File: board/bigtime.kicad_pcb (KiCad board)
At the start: 2 copper layers, 100 x 100 mm, 10 parts, among them IC1 NPIC6C596A, IC2 TPS62152, P1 CONN_IN, P2 CONN_OUT, U1 SA40-19

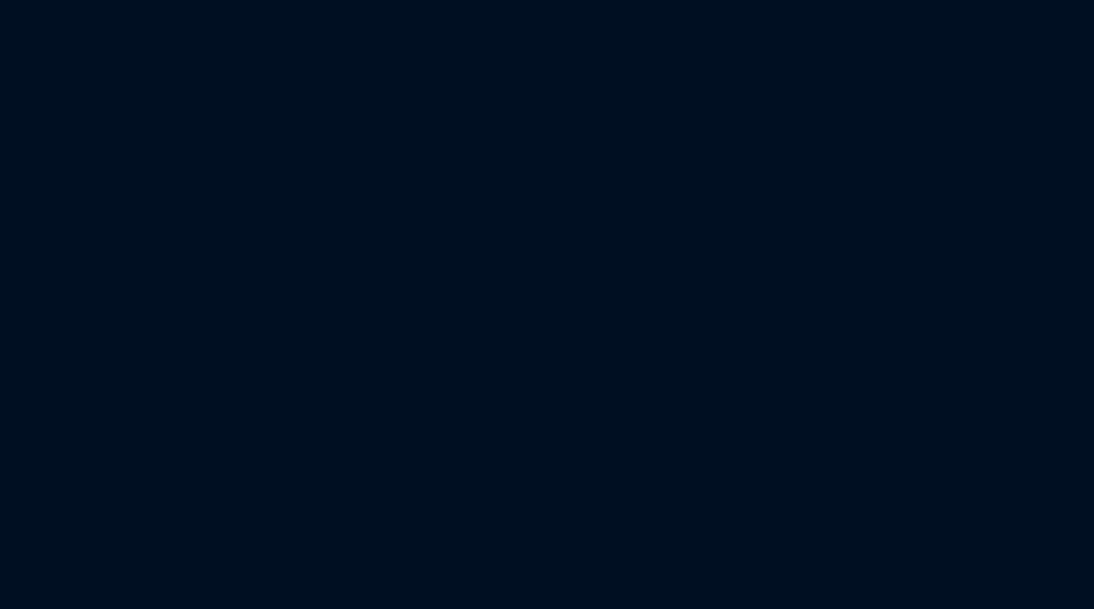
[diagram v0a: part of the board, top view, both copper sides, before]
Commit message: Added limit resistors
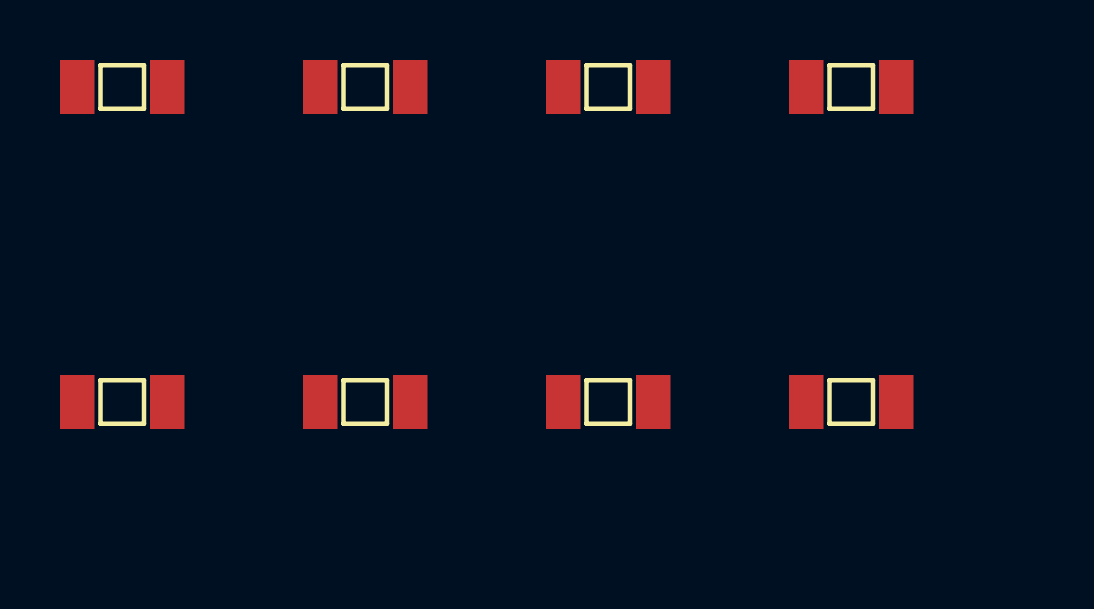
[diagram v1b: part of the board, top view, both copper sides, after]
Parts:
- added R1: 220R 500mW, agg:1206, F.Cu at (109.8, 43.9)
- added R2: 220R 500mW, agg:1206, F.Cu at (85.5, 43.9)
- added R3: 220R 500mW, agg:1206, F.Cu at (93.6, 33.4)
- added R4: 220R 500mW, agg:1206, F.Cu at (101.7, 33.4)
- added R5: 220R 500mW, agg:1206, F.Cu at (93.6, 43.9)
- added R6: 220R 500mW, agg:1206, F.Cu at (85.5, 33.4)
- added R7: 220R 500mW, agg:1206, F.Cu at (101.7, 43.9)
- added R8: 400R 500mW, agg:1206, F.Cu at (109.8, 33.4)
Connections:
- U1 pad 1: Net-(IC1-Pad11) -> Net-(R5-Pad1)
- U1 pad 10: Net-(IC1-Pad13) -> Net-(R7-Pad1)
- U1 pad 2: Net-(IC1-Pad6) -> Net-(R4-Pad1)
- U1 pad 4: Net-(IC1-Pad5) -> Net-(R3-Pad1)
- U1 pad 5: Net-(IC1-Pad14) -> Net-(R8-Pad2)
- U1 pad 6: Net-(IC1-Pad4) -> Net-(R2-Pad1)
- U1 pad 7: Net-(IC1-Pad3) -> Net-(R1-Pad1)
- U1 pad 9: Net-(IC1-Pad12) -> Net-(R6-Pad1)

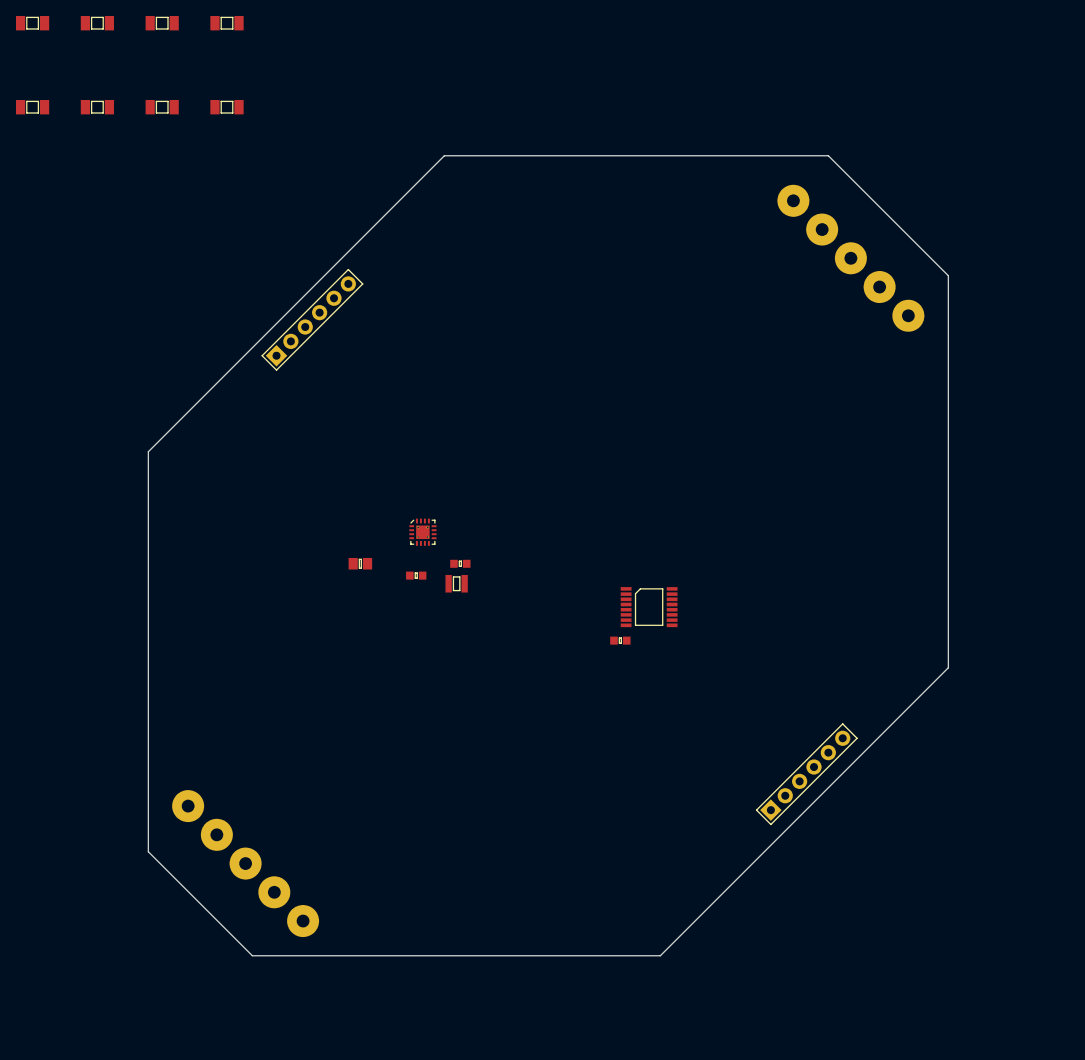
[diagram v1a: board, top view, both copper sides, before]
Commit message: Rectangular board because life's too short
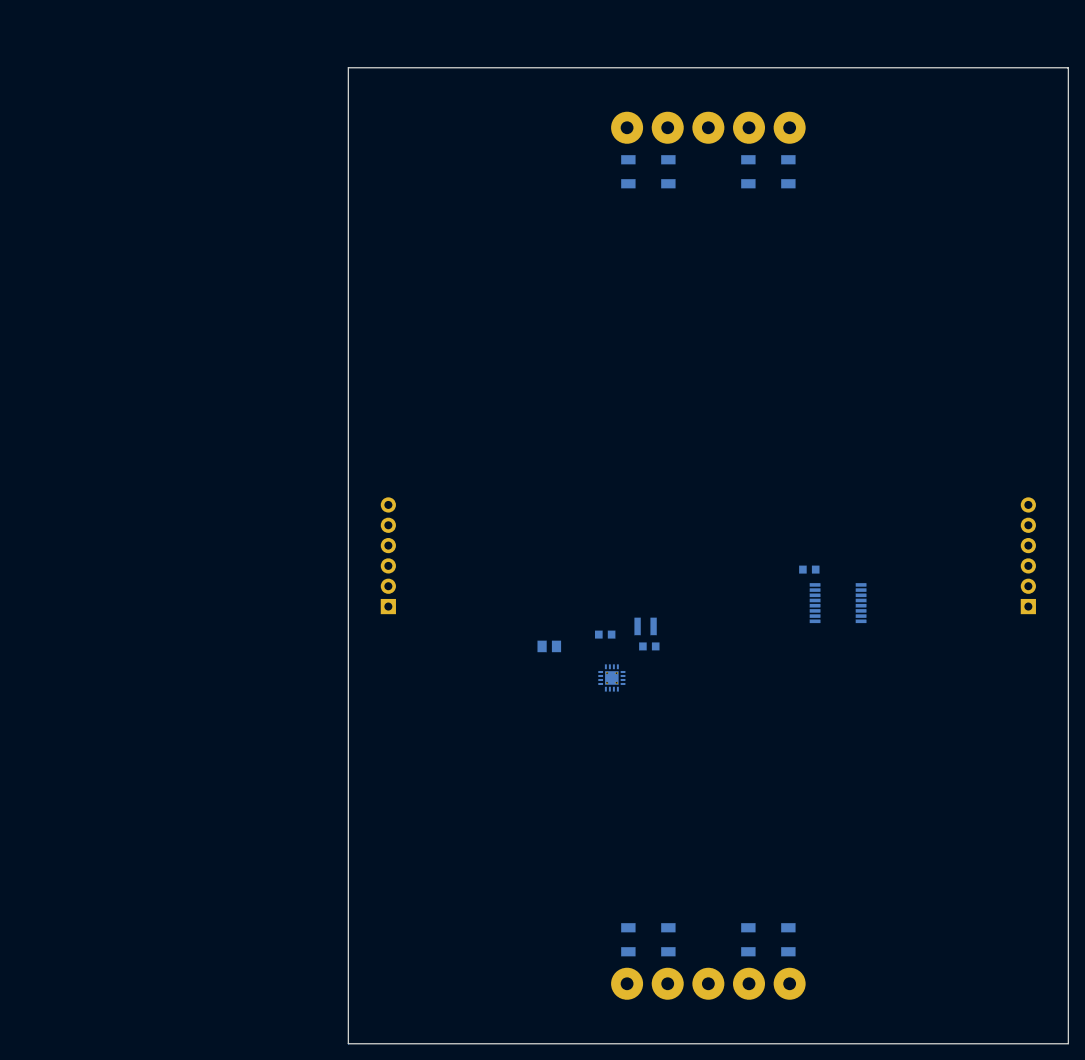
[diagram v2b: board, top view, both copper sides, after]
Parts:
- C1, C2, C3, C4, IC1, IC2, L1, P1, P2, R1, R2, R3, R4, R5, R6, R7, R8: moved to B.Cu
- moved R3 140.5 mm to (175.0, 148.0), turned to 90 degrees
- moved R8 134.4 mm to (180.0, 148.0), turned to 270 degrees
- moved R4 130.9 mm to (165.0, 148.0), turned to 90 degrees
- moved R5 123.4 mm to (160.0, 148.0), turned to 90 degrees
- moved R2 94.8 mm to (180.0, 52.0), turned to 270 degrees
- moved R6 81.6 mm to (165.0, 52.0), turned to 270 degrees
- moved R1 65.7 mm to (175.0, 52.0), turned to 270 degrees
- moved R7 58.8 mm to (160.0, 52.0), turned to 270 degrees
- moved P2 38.9 mm to (210.0, 100.0), turned to 90 degrees
- moved P1 31.0 mm to (130.0, 100.0), turned to 90 degrees
- moved IC2 29.8 mm to (157.9, 115.3)
- moved C3 25.8 mm to (162.6, 111.3)
- moved C4 25.8 mm to (150.1, 111.3)
- moved C1 25.2 mm to (182.6, 101.7)
- moved C2 24.7 mm to (157.1, 109.9)
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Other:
- board size 100 x 100 mm -> 90 x 122 mm

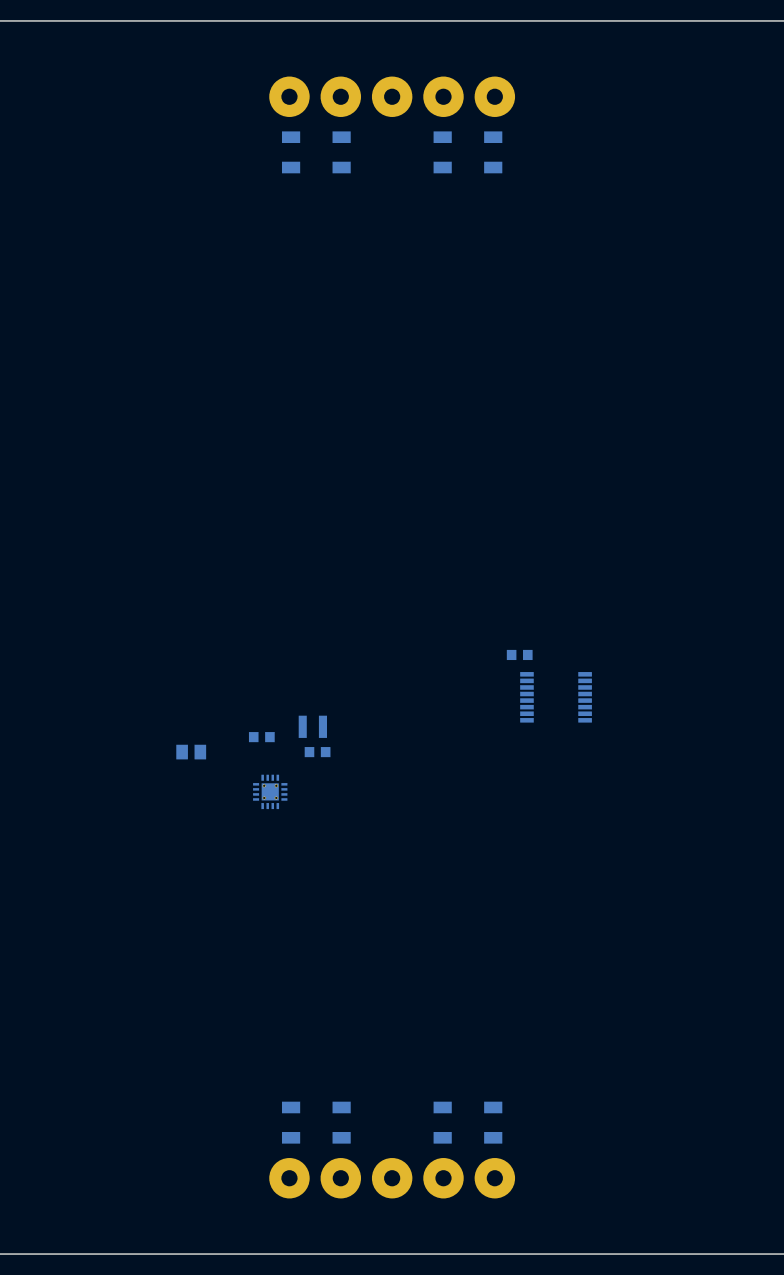
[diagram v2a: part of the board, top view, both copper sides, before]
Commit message: Don't forget the mounting holes!
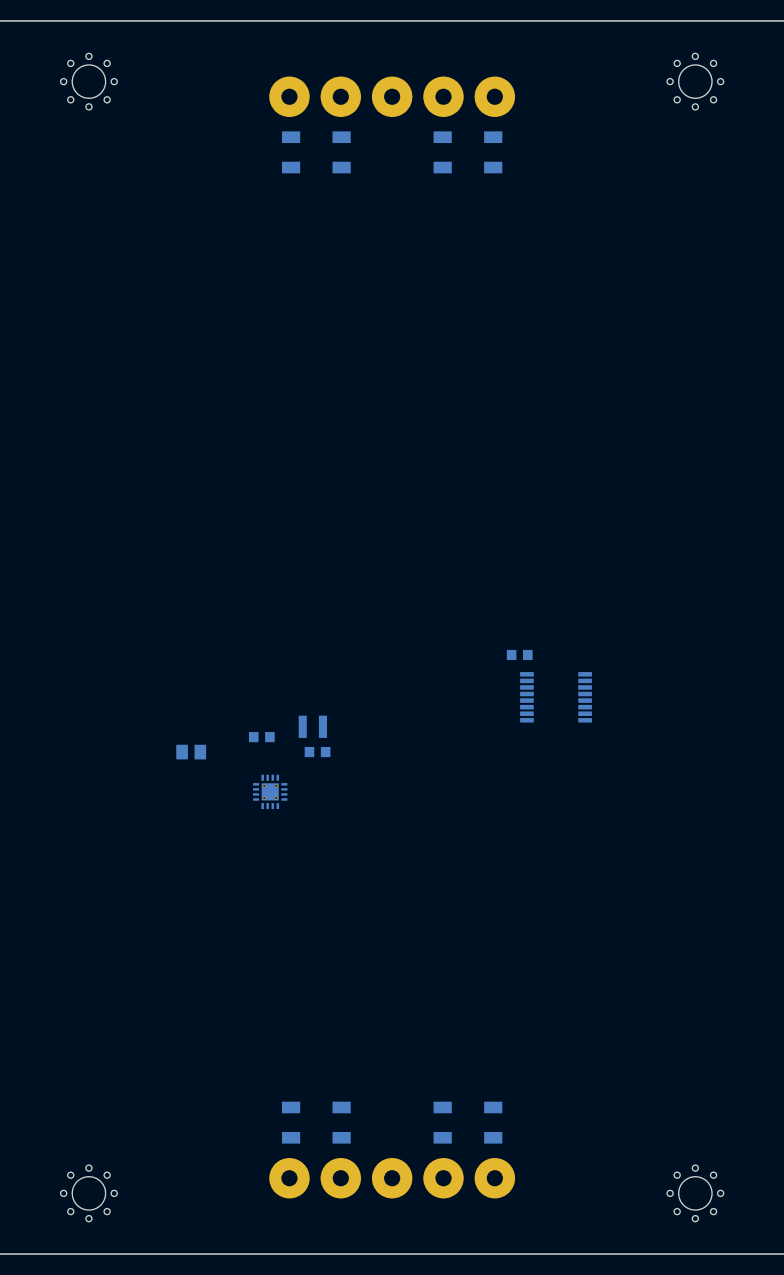
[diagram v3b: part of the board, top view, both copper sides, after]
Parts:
- added X1: MOUNTING_HOLE, agg:M3_MOUNT, F.Cu at (200.0, 155.0)
- added X2: MOUNTING_HOLE, agg:M3_MOUNT, F.Cu at (140.0, 45.0)
- added X3: MOUNTING_HOLE, agg:M3_MOUNT, F.Cu at (140.0, 155.0)
- added X4: MOUNTING_HOLE, agg:M3_MOUNT, F.Cu at (200.0, 45.0)
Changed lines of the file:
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@@
     (tracks 0)
     (zones 0)
-    (modules 18)
+    (modules 22)
     (nets 26)
   )
@@
     (add_net "Net-(R8-Pad2)")
   )
+  (module agg:M3_MOUNT (layer F.Cu)
+    (at 200 155)
+    (fp_text reference X1 (at 0 -4.1) (layer F.Fab) hide
+      (effects (font (size 1 1) (thickness 0.15)))
+    )
+    (fp_text value MOUNTING_HOLE (at 0 4.1) (layer F.Fab) hide
+      (effects (font (size 1 1) (thickness 0.15)))
+    )
+    (fp_line (start -3.4 -3.4) (end 3.4 -3.4) (layer F.CrtYd) (width 0.01))
+    (fp_line (start 3.4 -3.4) (end 3.4 3.4) (layer F.CrtYd) (width 0.01))
+    (fp_line (start 3.4 3.4) (end -3.4 3.4) (layer F.CrtYd) (width 0.01))
+    (fp_line (start -3.4 3.4) (end -3.4 -3.4) (layer F.CrtYd) (width 0.01))
+    (pad "" np_thru_hole circle (at 1.8 1.8) (size 0.6 0.6) (drill 0.6) (layers *.Cu *.Mask F.SilkS))
+    (pad "" np_thru_hole circle (at -1.8 1.8) (size 0.6 0.6) (drill 0.6) (layers *.Cu *.Mask F.SilkS))
+    (pad "" np_thru_hole circle (at 1.8 -1.8) (size 0.6 0.6) (drill 0.6) (layers *.Cu *.Mask F.SilkS))
+    (pad "" np_thru_hole circle (at -1.8 -1.8) (size 0.6 0.6) (drill 0.6) (layers *.Cu *.Mask F.SilkS))
+    (pad "" np_thru_hole circle (at -2.5 0) (size 0.6 0.6) (drill 0.6) (layers *.Cu *.Mask F.SilkS))
+    (pad "" np_thru_hole circle (at 0 2.5) (size 0.6 0.6) (drill 0.6) (layers *.Cu *.Mask F.SilkS))
+    (pad "" np_thru_hole circle (at 2.5 0) (size 0.6 0.6) (drill 0.6) (layers *.Cu *.Mask F.SilkS))
+    (pad "" np_thru_hole circle (at 0 -2.5) (size 0.6 0.6) (drill 0.6) (layers *.Cu *.Mask F.SilkS))
+    (pad "" np_thru_hole circle (at 0 0) (size 3.3 3.3) (drill 3.3) (layers *.Cu *.Mask F.SilkS)
+      (solder_mask_margin 1.5) (clearance 1.65))
+  )
+  (module agg:M3_MOUNT (layer F.Cu)
+    (at 140 45)
+    (fp_text reference X2 (at 0 -4.1) (layer F.Fab) hide
+      (effects (font (size 1 1) (thickness 0.15)))
+    )
+    (fp_text value MOUNTING_HOLE (at 0 4.1) (layer F.Fab) hide
+      (effects (font (size 1 1) (thickness 0.15)))
+    )
+    (fp_line (start -3.4 3.4) (end -3.4 -3.4) (layer F.CrtYd) (width 0.01))
+    (fp_line (start 3.4 3.4) (end -3.4 3.4) (layer F.CrtYd) (width 0.01))
+    (fp_line (start 3.4 -3.4) (end 3.4 3.4) (layer F.CrtYd) (width 0.01))
+    (fp_line (start -3.4 -3.4) (end 3.4 -3.4) (layer F.CrtYd) (width 0.01))
+    (pad "" np_thru_hole circle (at 0 0) (size 3.3 3.3) (drill 3.3) (layers *.Cu *.Mask F.SilkS)
+      (solder_mask_margin 1.5) (clearance 1.65))
+    (pad "" np_thru_hole circle (at 0 -2.5) (size 0.6 0.6) (drill 0.6) (layers *.Cu *.Mask F.SilkS))
+    (pad "" np_thru_hole circle (at 2.5 0) (size 0.6 0.6) (drill 0.6) (layers *.Cu *.Mask F.SilkS))
+    (pad "" np_thru_hole circle (at 0 2.5) (size 0.6 0.6) (drill 0.6) (layers *.Cu *.Mask F.SilkS))
+    (pad "" np_thru_hole circle (at -2.5 0) (size 0.6 0.6) (drill 0.6) (layers *.Cu *.Mask F.SilkS))
+    (pad "" np_thru_hole circle (at -1.8 -1.8) (size 0.6 0.6) (drill 0.6) (layers *.Cu *.Mask F.SilkS))
+    (pad "" np_thru_hole circle (at 1.8 -1.8) (size 0.6 0.6) (drill 0.6) (layers *.Cu *.Mask F.SilkS))
+    (pad "" np_thru_hole circle (at -1.8 1.8) (size 0.6 0.6) (drill 0.6) (layers *.Cu *.Mask F.SilkS))
+    (pad "" np_thru_hole circle (at 1.8 1.8) (size 0.6 0.6) (drill 0.6) (layers *.Cu *.Mask F.SilkS))
+  )
+  (module agg:M3_MOUNT (layer F.Cu)
+    (at 140 155)
+    (fp_text reference X3 (at 0 -4.1) (layer F.Fab) hide
+      (effects (font (size 1 1) (thickness 0.15)))
+    )
+    (fp_text value MOUNTING_HOLE (at 0 4.1) (layer F.Fab) hide
+      (effects (font (size 1 1) (thickness 0.15)))
+    )
+    (fp_line (start -3.4 -3.4) (end 3.4 -3.4) (layer F.CrtYd) (width 0.01))
+    (fp_line (start 3.4 -3.4) (end 3.4 3.4) (layer F.CrtYd) (width 0.01))
+    (fp_line (start 3.4 3.4) (end -3.4 3.4) (layer F.CrtYd) (width 0.01))
+    (fp_line (start -3.4 3.4) (end -3.4 -3.4) (layer F.CrtYd) (width 0.01))
+    (pad "" np_thru_hole circle (at 1.8 1.8) (size 0.6 0.6) (drill 0.6) (layers *.Cu *.Mask F.SilkS))
+    (pad "" np_thru_hole circle (at -1.8 1.8) (size 0.6 0.6) (drill 0.6) (layers *.Cu *.Mask F.SilkS))
+    (pad "" np_thru_hole circle (at 1.8 -1.8) (size 0.6 0.6) (drill 0.6) (layers *.Cu *.Mask F.SilkS))
+    (pad "" np_thru_hole circle (at -1.8 -1.8) (size 0.6 0.6) (drill 0.6) (layers *.Cu *.Mask F.SilkS))
+    (pad "" np_thru_hole circle (at -2.5 0) (size 0.6 0.6) (drill 0.6) (layers *.Cu *.Mask F.SilkS))
+    (pad "" np_thru_hole circle (at 0 2.5) (size 0.6 0.6) (drill 0.6) (layers *.Cu *.Mask F.SilkS))
+    (pad "" np_thru_hole circle (at 2.5 0) (size 0.6 0.6) (drill 0.6) (layers *.Cu *.Mask F.SilkS))
+    (pad "" np_thru_hole circle (at 0 -2.5) (size 0.6 0.6) (drill 0.6) (layers *.Cu *.Mask F.SilkS))
+    (pad "" np_thru_hole circle (at 0 0) (size 3.3 3.3) (drill 3.3) (layers *.Cu *.Mask F.SilkS)
+      (solder_mask_margin 1.5) (clearance 1.65))
+  )
+  (module agg:M3_MOUNT (layer F.Cu)
+    (at 200 45)
+    (fp_text reference X4 (at 0 -4.1) (layer F.Fab) hide
+      (effects (font (size 1 1) (thickness 0.15)))
+    )
+    (fp_text value MOUNTING_HOLE (at 0 4.1) (layer F.Fab) hide
+      (effects (font (size 1 1) (thickness 0.15)))
+    )
+    (fp_line (start -3.4 3.4) (end -3.4 -3.4) (layer F.CrtYd) (width 0.01))
+    (fp_line (start 3.4 3.4) (end -3.4 3.4) (layer F.CrtYd) (width 0.01))
+    (fp_line (start 3.4 -3.4) (end 3.4 3.4) (layer F.CrtYd) (width 0.01))
+    (fp_line (start -3.4 -3.4) (end 3.4 -3.4) (layer F.CrtYd) (width 0.01))
+    (pad "" np_thru_hole circle (at 0 0) (size 3.3 3.3) (drill 3.3) (layers *.Cu *.Mask F.SilkS)
+      (solder_mask_margin 1.5) (clearance 1.65))
+    (pad "" np_thru_hole circle (at 0 -2.5) (size 0.6 0.6) (drill 0.6) (layers *.Cu *.Mask F.SilkS))
+    (pad "" np_thru_hole circle (at 2.5 0) (size 0.6 0.6) (drill 0.6) (layers *.Cu *.Mask F.SilkS))
+    (pad "" np_thru_hole circle (at 0 2.5) (size 0.6 0.6) (drill 0.6) (layers *.Cu *.Mask F.SilkS))
+    (pad "" np_thru_hole circle (at -2.5 0) (size 0.6 0.6) (drill 0.6) (layers *.Cu *.Mask F.SilkS))
+    (pad "" np_thru_hole circle (at -1.8 -1.8) (size 0.6 0.6) (drill 0.6) (layers *.Cu *.Mask F.SilkS))
+    (pad "" np_thru_hole circle (at 1.8 -1.8) (size 0.6 0.6) (drill 0.6) (layers *.Cu *.Mask F.SilkS))
+    (pad "" np_thru_hole circle (at -1.8 1.8) (size 0.6 0.6) (drill 0.6) (layers *.Cu *.Mask F.SilkS))
+    (pad "" np_thru_hole circle (at 1.8 1.8) (size 0.6 0.6) (drill 0.6) (layers *.Cu *.Mask F.SilkS))
+  )
   (module footprints:SA40-18 (layer F.Cu)
